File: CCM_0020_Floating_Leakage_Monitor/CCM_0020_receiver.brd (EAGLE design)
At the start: 76.2 x 76.2 mm, 91 parts, among them IC1 AD8656R, IC10 LF356D, IC11 LF356D, IC2 LM311D, IC3 LT1495, IC4 741G00, IC5 741G04, IC6 741G04, IC7 741G04, IC8 AD820R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

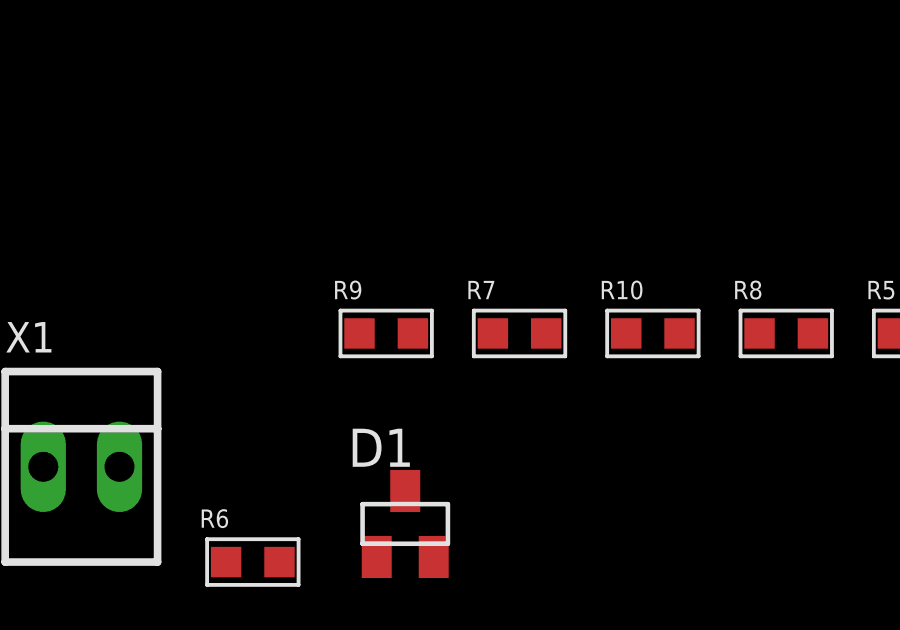
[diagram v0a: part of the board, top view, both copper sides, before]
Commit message: Simplified leakage monitor receiver.
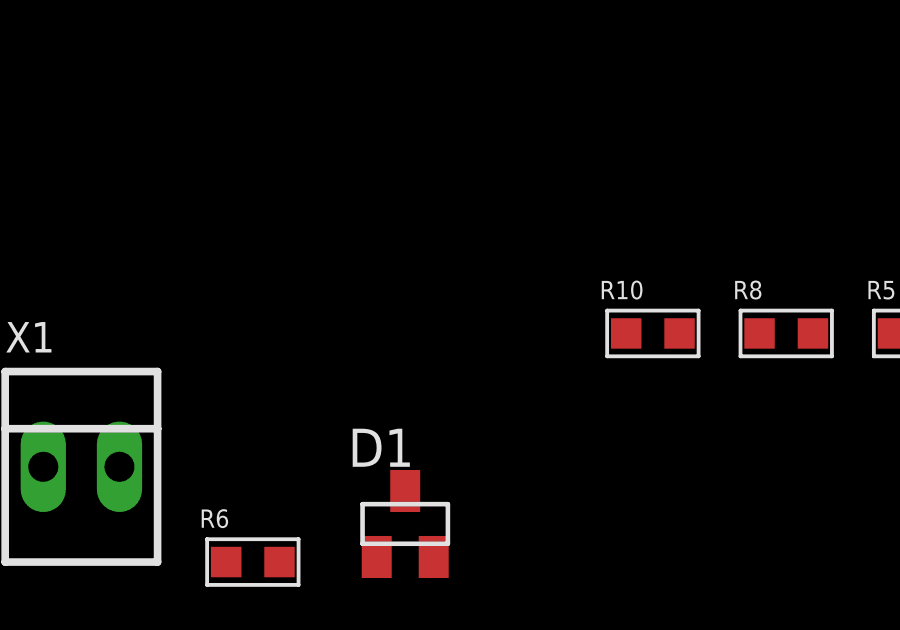
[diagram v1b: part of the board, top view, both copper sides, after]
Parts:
- removed R7: 30k, acrooptics:0603
- removed R9: 20k, acrooptics:0603
- D1: value LM4040-2.5V -> MAX6006
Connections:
- removed net N$9: IC2.3, R7.2, R9.1
- net GND: no longer R9.2
- net N$14: now also IC2.3; no longer R7.1
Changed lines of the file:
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@@
 <?xml version="1.0" encoding="utf-8"?>
 <!DOCTYPE eagle SYSTEM "eagle.dtd">
-<eagle version="9.4.2">
+<eagle version="9.3.2">
 <drawing>
 <settings>
@@
 <attribute name="VALUE" x="-361.696" y="-453.263" size="0.6096" layer="27" font="vector" ratio="20"/>
 </element>
-<element name="R7" library="acrooptics" package="0603" value="30k" x="-364.49" y="-451.485" smashed="yes">
-<attribute name="NAME" x="-366.268" y="-450.342" size="0.6096" layer="25" font="vector" ratio="20"/>
-<attribute name="VALUE" x="-366.141" y="-453.263" size="0.6096" layer="27" font="vector" ratio="20"/>
-</element>
-<element name="R9" library="acrooptics" package="0603" value="20k" x="-368.935" y="-451.485" smashed="yes">
-<attribute name="NAME" x="-370.713" y="-450.342" size="0.6096" layer="25" font="vector" ratio="20"/>
-<attribute name="VALUE" x="-370.586" y="-453.263" size="0.6096" layer="27" font="vector" ratio="20"/>
-</element>
-<element name="D1" library="noah" package="SOT23" value="LM4040-2.5V" x="-368.3" y="-457.835" smashed="yes">
+<element name="D1" library="noah" package="SOT23" value="MAX6006" x="-368.3" y="-457.835" smashed="yes">
 <attribute name="NAME" x="-370.205" y="-455.93" size="1.27" layer="25"/>
 <attribute name="VALUE" x="-370.205" y="-461.01" size="1.27" layer="27"/>
@@
 <contactref element="IC2" pad="1"/>
 <contactref element="D1" pad="2"/>
-<contactref element="R9" pad="2"/>
 <contactref element="X1" pad="2"/>
 <contactref element="U1" pad="4"/>
@@
 <wire x1="-384.81" y1="-454.5838" x2="-387.35" y2="-459.8162" width="0" layer="19" extent="1-1"/>
 <wire x1="-377.825" y1="-455.93" x2="-384.81" y2="-454.5838" width="0" layer="19" extent="1-1"/>
-<wire x1="-368.046" y1="-451.485" x2="-377.825" y2="-455.93" width="0" layer="19" extent="1-1"/>
-<wire x1="-367.35" y1="-458.935" x2="-368.046" y2="-451.485" width="0" layer="19" extent="1-1"/>
-<wire x1="-334.391" y1="-451.485" x2="-368.046" y2="-451.485" width="0" layer="19" extent="1-1"/>
+<wire x1="-367.35" y1="-458.935" x2="-377.825" y2="-455.93" width="0" layer="19" extent="1-1"/>
+<wire x1="-334.391" y1="-451.485" x2="-367.35" y2="-458.935" width="0" layer="19" extent="1-1"/>
 <wire x1="-325.501" y1="-451.485" x2="-334.391" y2="-451.485" width="0" layer="19" extent="1-1"/>
 <wire x1="-298.45" y1="-442.655" x2="-325.501" y2="-451.485" width="0" layer="19" extent="1-1"/>
@@
 <contactref element="R6" pad="2"/>
 <contactref element="D1" pad="1"/>
-<contactref element="R7" pad="1"/>
-<wire x1="-369.25" y1="-458.935" x2="-372.491" y2="-459.105" width="0" layer="19" extent="1-1"/>
-<wire x1="-365.379" y1="-451.485" x2="-369.25" y2="-458.935" width="0" layer="19" extent="1-1"/>
-</signal>
-<signal name="N$9">
-<contactref element="R7" pad="2"/>
-<contactref element="R9" pad="1"/>
 <contactref element="IC2" pad="3"/>
-<wire x1="-363.601" y1="-451.485" x2="-295.91" y2="-442.655" width="0" layer="19" extent="1-1"/>
-<wire x1="-369.824" y1="-451.485" x2="-363.601" y2="-451.485" width="0" layer="19" extent="1-1"/>
+<wire x1="-369.25" y1="-458.935" x2="-295.91" y2="-442.655" width="0" layer="19" extent="1-1"/>
+<wire x1="-372.491" y1="-459.105" x2="-369.25" y2="-458.935" width="0" layer="19" extent="1-1"/>
 </signal>
 <signal name="N$7">
